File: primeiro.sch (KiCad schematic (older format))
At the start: 5 parts

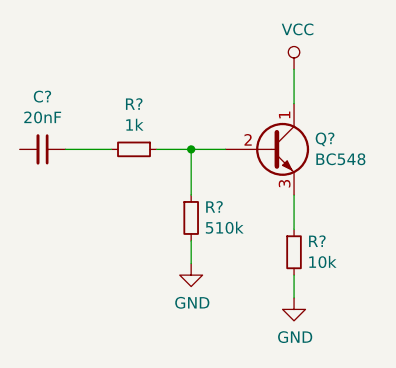
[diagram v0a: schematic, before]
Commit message: adicionei as footprints
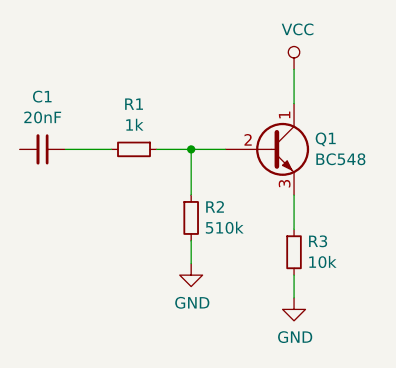
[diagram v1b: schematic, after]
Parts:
- C1: renamed from C?; footprint (none) -> Capacitor_THT:C_Disc_D3.0mm_W2.0mm_P2.50mm
- R1, R2, R3: renamed from R?; footprint (none) -> Resistor_THT:R_Axial_DIN0204_L3.6mm_D1.6mm_P7.62mm_Horizontal
- gave numbers to parts that had none: 1
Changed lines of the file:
@@
 $EndDescr
 $Comp
-L Device:R_Small R?
+L Device:R_Small R1
 U 1 1 5D4E65C3
 P 5100 4050
-F 0 "R?" V 4904 4050 50  0000 C CNN
+F 0 "R1" V 4904 4050 50  0000 C CNN
 F 1 "1k" V 4995 4050 50  0000 C CNN
-F 2 "" H 5100 4050 50  0001 C CNN
+F 2 "Resistor_THT:R_Axial_DIN0204_L3.6mm_D1.6mm_P7.62mm_Horizontal" H 5100 4050 50  0001 C CNN
 F 3 "~" H 5100 4050 50  0001 C CNN
 	1    5100 4050
@@
 $EndComp
 $Comp
-L Device:R_Small R?
+L Device:R_Small R2
 U 1 1 5D4E705B
 P 5350 4350
-F 0 "R?" H 5409 4396 50  0000 L CNN
+F 0 "R2" H 5409 4396 50  0000 L CNN
 F 1 "510k" H 5409 4305 50  0000 L CNN
-F 2 "" H 5350 4350 50  0001 C CNN
+F 2 "Resistor_THT:R_Axial_DIN0204_L3.6mm_D1.6mm_P7.62mm_Horizontal" H 5350 4350 50  0001 C CNN
 F 3 "~" H 5350 4350 50  0001 C CNN
 	1    5350 4350
@@
 $EndComp
 $Comp
-L Device:R_Small R?
+L Device:R_Small R3
 U 1 1 5D4E758E
 P 5800 4500
-F 0 "R?" H 5859 4546 50  0000 L CNN
+F 0 "R3" H 5859 4546 50  0000 L CNN
 F 1 "10k" H 5859 4455 50  0000 L CNN
-F 2 "" H 5800 4500 50  0001 C CNN
+F 2 "Resistor_THT:R_Axial_DIN0204_L3.6mm_D1.6mm_P7.62mm_Horizontal" H 5800 4500 50  0001 C CNN
 F 3 "~" H 5800 4500 50  0001 C CNN
 	1    5800 4500
@@
 $EndComp
 $Comp
-L Device:C_Small C?
+L Device:C_Small C1
 U 1 1 5D4E7B2D
 P 4700 4050
-F 0 "C?" V 4471 4050 50  0000 C CNN
+F 0 "C1" V 4471 4050 50  0000 C CNN
 F 1 "20nF" V 4562 4050 50  0000 C CNN
-F 2 "" H 4700 4050 50  0001 C CNN
+F 2 "Capacitor_THT:C_Disc_D3.0mm_W2.0mm_P2.50mm" H 4700 4050 50  0001 C CNN
 F 3 "~" H 4700 4050 50  0001 C CNN
 	1    4700 4050
@@
 $EndComp
 $Comp
-L Transistor_BJT:BC548 Q?
+L Transistor_BJT:BC548 Q1
 U 1 1 5D4E875A
 P 5700 4050
-F 0 "Q?" H 5891 4096 50  0000 L CNN
+F 0 "Q1" H 5891 4096 50  0000 L CNN
 F 1 "BC548" H 5891 4005 50  0000 L CNN
 F 2 "Package_TO_SOT_THT:TO-92_Inline" H 5900 3975 50  0001 L CIN
@@
 $EndComp
 $Comp
-L power:GND #PWR?
+L power:GND #PWR0101
 U 1 1 5D4E96FB
 P 5800 4700
-F 0 "#PWR?" H 5800 4450 50  0001 C CNN
+F 0 "#PWR0101" H 5800 4450 50  0001 C CNN
 F 1 "GND" H 5805 4527 50  0000 C CNN
 F 2 "" H 5800 4700 50  0001 C CNN
@@
 $EndComp
 $Comp
-L power:VCC #PWR?
+L power:VCC #PWR0102
 U 1 1 5D4E9BAA
 P 5800 3700
-F 0 "#PWR?" H 5800 3550 50  0001 C CNN
+F 0 "#PWR0102" H 5800 3550 50  0001 C CNN
 F 1 "VCC" H 5817 3873 50  0000 C CNN
 F 2 "" H 5800 3700 50  0001 C CNN
@@
 	5800 3850 5800 3700
 $Comp
-L power:GND #PWR?
+L power:GND #PWR0103
 U 1 1 5D4EC429
 P 5350 4550
-F 0 "#PWR?" H 5350 4300 50  0001 C CNN
+F 0 "#PWR0103" H 5350 4300 50  0001 C CNN
 F 1 "GND" H 5355 4377 50  0000 C CNN
 F 2 "" H 5350 4550 50  0001 C CNN
